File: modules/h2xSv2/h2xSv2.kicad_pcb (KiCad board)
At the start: 2 copper layers, 40.6 x 40.6 mm, 14 parts, among them J1 Conn_01x10_Male, J10 Conn_01x02_Male, J2 Conn_01x10_Male, J3 Conn_01x10_Male, J4 Conn_01x10_Male, J5 Conn_01x04_Male, J6 Conn_01x04_Male, J7 Conn_01x12_Male, J8 Conn_01x12_Male, J9 Conn_01x12_Male

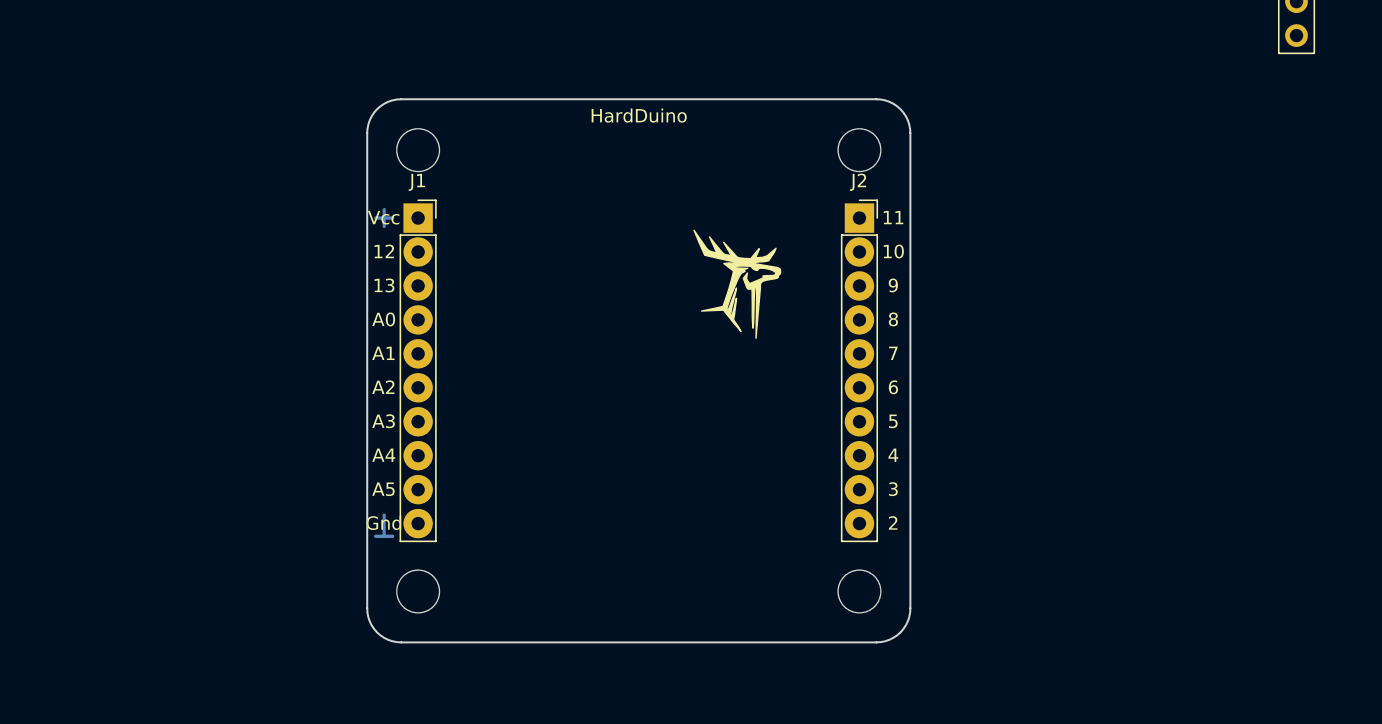
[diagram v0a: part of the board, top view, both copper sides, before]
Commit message: Fix holes and edges
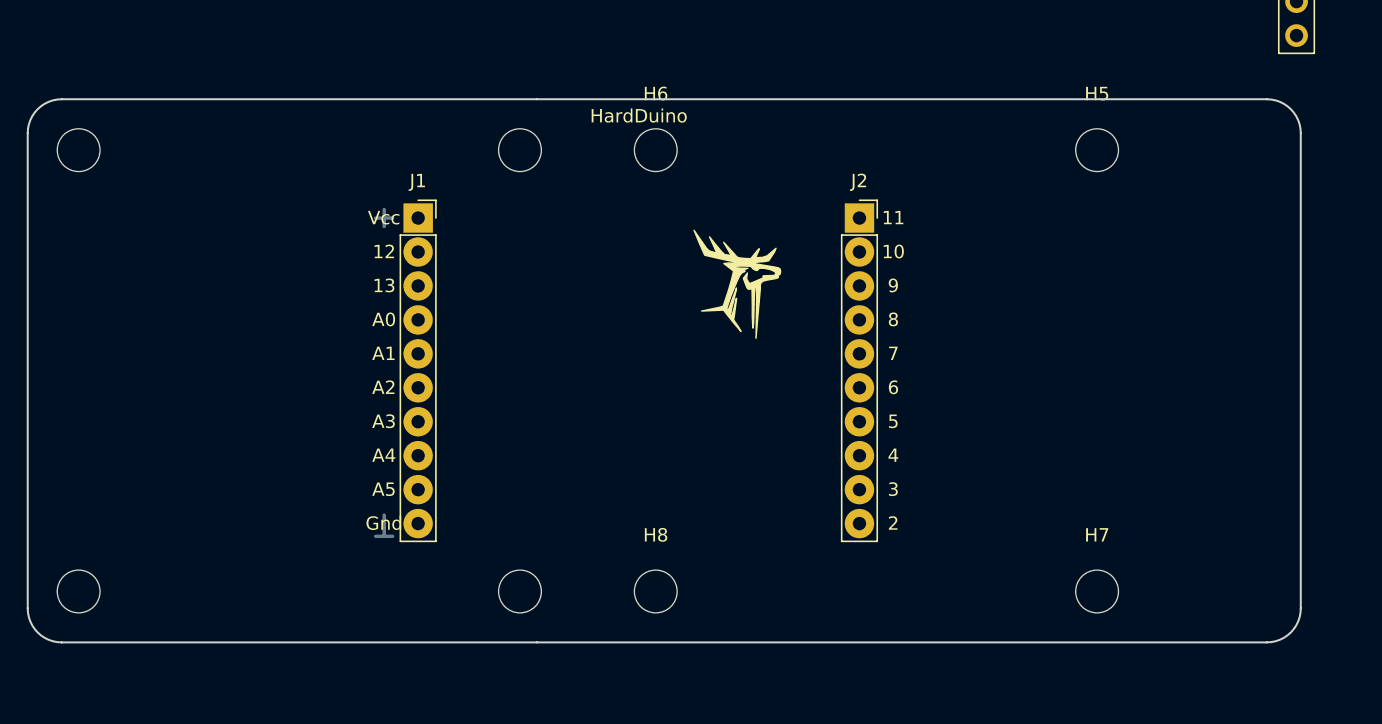
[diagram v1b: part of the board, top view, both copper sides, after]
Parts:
- added H5: MountingHole, MountingHole:MountingHole_3.2mm_M3, F.Cu at (143.5, 54.6)
- added H6: MountingHole, MountingHole:MountingHole_3.2mm_M3, F.Cu at (110.5, 54.6)
- added H7: MountingHole, MountingHole:MountingHole_3.2mm_M3, F.Cu at (143.5, 87.6)
- added H8: MountingHole, MountingHole:MountingHole_3.2mm_M3, F.Cu at (110.5, 87.6)
- moved H3 58.4 mm to (67.3, 54.6), turned to 90 degrees
- moved H4 41.7 mm to (100.3, 54.6), turned to 90 degrees
- moved H1 41.7 mm to (67.3, 87.6), turned to 90 degrees
- moved H2 7.62 mm to (100.3, 87.6), turned to 90 degrees
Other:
- board size 40.6 x 40.6 mm -> 95.2 x 40.6 mm
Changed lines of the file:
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@@
   (general
     (thickness 1.6)
-    (drawings 30)
+    (drawings 32)
     (tracks 4)
     (zones 0)
-    (modules 14)
+    (modules 18)
     (nets 21)
   )
@@
   )
   (module MountingHole:MountingHole_3.2mm_M3 (layer F.Cu)
-    (at 92.71 54.61)
+    (at 67.31 87.63 90)
     (descr "Mounting Hole 3.2mm, no annular, M3")
     (tags "mounting hole 3.2mm no annular m3")
@@
   )
   (module MountingHole:MountingHole_3.2mm_M3 (layer F.Cu)
-    (at 92.71 87.63)
+    (at 100.33 87.63 90)
     (descr "Mounting Hole 3.2mm, no annular, M3")
     (tags "mounting hole 3.2mm no annular m3")
@@
   )
   (module MountingHole:MountingHole_3.2mm_M3 (layer F.Cu)
-    (at 125.73 54.61)
+    (at 67.31 54.61 90)
     (descr "Mounting Hole 3.2mm, no annular, M3")
     (tags "mounting hole 3.2mm no annular m3")
@@
   )
   (module MountingHole:MountingHole_3.2mm_M3 (layer F.Cu)
-    (at 125.73 87.63)
+    (at 100.33 54.61 90)
     (descr "Mounting Hole 3.2mm, no annular, M3")
     (tags "mounting hole 3.2mm no annular m3")
@@
     )
   )
+  (module MountingHole:MountingHole_3.2mm_M3 (layer F.Cu)
+    (at 143.51 54.61)
+    (descr "Mounting Hole 3.2mm, no annular, M3")
+    (tags "mounting hole 3.2mm no annular m3")
+    (attr virtual)
+    (fp_text reference H5 (at 0 -4.2) (layer F.SilkS)
+      (effects (font (size 1 1) (thickness 0.15)))
+    )
+    (fp_text value MountingHole (at 0 4.2) (layer F.Fab)
+      (effects (font (size 1 1) (thickness 0.15)))
+    )
+    (fp_circle (center 0 0) (end 3.45 0) (layer F.CrtYd) (width 0.05))
+    (fp_circle (center 0 0) (end 3.2 0) (layer Cmts.User) (width 0.15))
+    (fp_text user %R (at 0.3 0) (layer F.Fab)
+      (effects (font (size 1 1) (thickness 0.15)))
+    )
+    (pad 1 np_thru_hole circle (at 0 0) (size 3.2 3.2) (drill 3.2) (layers *.Cu *.Mask))
+  )
+  (module MountingHole:MountingHole_3.2mm_M3 (layer F.Cu)
+    (at 110.49 54.61)
+    (descr "Mounting Hole 3.2mm, no annular, M3")
+    (tags "mounting hole 3.2mm no annular m3")
+    (attr virtual)
+    (fp_text reference H6 (at 0 -4.2) (layer F.SilkS)
+      (effects (font (size 1 1) (thickness 0.15)))
+    )
+    (fp_text value MountingHole (at 0 4.2) (layer F.Fab)
+      (effects (font (size 1 1) (thickness 0.15)))
+    )
+    (fp_text user %R (at 0.3 0) (layer F.Fab)
+      (effects (font (size 1 1) (thickness 0.15)))
+    )
+    (fp_circle (center 0 0) (end 3.2 0) (layer Cmts.User) (width 0.15))
+    (fp_circle (center 0 0) (end 3.45 0) (layer F.CrtYd) (width 0.05))
+    (pad 1 np_thru_hole circle (at 0 0) (size 3.2 3.2) (drill 3.2) (layers *.Cu *.Mask))
+  )
+  (module MountingHole:MountingHole_3.2mm_M3 (layer F.Cu)
+    (at 143.51 87.63)
+    (descr "Mounting Hole 3.2mm, no annular, M3")
+    (tags "mounting hole 3.2mm no annular m3")
+    (attr virtual)
+    (fp_text reference H7 (at 0 -4.2) (layer F.SilkS)
+      (effects (font (size 1 1) (thickness 0.15)))
+    )
+    (fp_text value MountingHole (at 0 4.2) (layer F.Fab)
+      (effects (font (size 1 1) (thickness 0.15)))
+    )
+    (fp_circle (center 0 0) (end 3.45 0) (layer F.CrtYd) (width 0.05))
+    (fp_circle (center 0 0) (end 3.2 0) (layer Cmts.User) (width 0.15))
+    (fp_text user %R (at 0.3 0) (layer F.Fab)
+      (effects (font (size 1 1) (thickness 0.15)))
+    )
+    (pad 1 np_thru_hole circle (at 0 0) (size 3.2 3.2) (drill 3.2) (layers *.Cu *.Mask))
+  )
+  (module MountingHole:MountingHole_3.2mm_M3 (layer F.Cu)
+    (at 110.49 87.63)
+    (descr "Mounting Hole 3.2mm, no annular, M3")
+    (tags "mounting hole 3.2mm no annular m3")
+    (attr virtual)
+    (fp_text reference H8 (at 0 -4.2) (layer F.SilkS)
+      (effects (font (size 1 1) (thickness 0.15)))
+    )
+    (fp_text value MountingHole (at 0 4.2) (layer F.Fab)
+      (effects (font (size 1 1) (thickness 0.15)))
+    )
+    (fp_text user %R (at 0.3 0) (layer F.Fab)
+      (effects (font (size 1 1) (thickness 0.15)))
+    )
+    (fp_circle (center 0 0) (end 3.2 0) (layer Cmts.User) (width 0.15))
+    (fp_circle (center 0 0) (end 3.45 0) (layer F.CrtYd) (width 0.05))
+    (pad 1 np_thru_hole circle (at 0 0) (size 3.2 3.2) (drill 3.2) (layers *.Cu *.Mask))
+  )
   (gr_poly (pts (xy 113.35 60.6) (xy 114.06 61.62) (xy 114.28 61.94) (xy 114.47 62.12) (xy 114.53 62.16) (xy 114.96 62.29) (xy 115 62.27) (xy 115 62.18) (xy 114.81 61.75) (xy 114.51 61.1) (xy 115.32 62.09) (xy 115.52 62.31) (xy 115.64 62.41) (xy 115.72 62.44) (xy 115.9 62.45) (xy 116.12 62.51) (xy 116.08 62.39) (xy 115.57 61.5) (xy 116.34 62.34) (xy 116.5 62.53) (xy 116.59 62.61) (xy 116.7 62.66) (xy 117.14 62.71) (xy 117.6 62.73) (xy 118.08 62.13) (xy 118.23 61.98) (xy 118.22 62.06) (xy 118.08 62.39) (xy 118 62.56) (xy 117.99 62.64) (xy 118.07 62.65) (xy 118.47 62.63) (xy 118.82 62.52) (xy 119.49 61.95) (xy 119.37 62.24) (xy 118.94 62.89) (xy 118.61 62.95) (xy 118 63) (xy 117.81 63.07) (xy 118.03 63.13) (xy 119.36 63.35) (xy 119.68 63.42) (xy 119.81 63.52) (xy 119.83 63.69) (xy 119.81 63.85) (xy 119.75 63.93) (xy 119.7 63.95) (xy 119.66 64.03) (xy 119.66 64.13) (xy 119.6 64.18) (xy 119.41 64.23) (xy 118.79 64.34) (xy 118.5 64.42) (xy 118.37 64.54) (xy 118.34 64.6) (xy 118.31 64.75) (xy 118.32 64.92) (xy 117.99 68.69) (xy 118.04 65.3) (xy 118.03 65.02) (xy 118.02 64.83) (xy 118.01 64.79) (xy 117.97 64.75) (xy 117.92 64.87) (xy 117.89 65.2) (xy 117.86 65.69) (xy 117.83 67.07) (xy 117.81 67.6) (xy 117.77 67.93) (xy 117.74 67.75) (xy 117.71 67.07) (xy 117.71 66.19) (xy 117.69 64.97) (xy 117.53 65.01) (xy 117.42 65.01) (xy 117.35 64.96) (xy 117.28 64.83) (xy 117.04 64.2) (xy 117.35 63.8) (xy 117.31 64.03) (xy 117.3 64.19) (xy 117.3 64.26) (xy 117.37 64.39) (xy 117.52 64.6) (xy 118.43 64.21) (xy 118.56 64.14) (xy 118.61 64.08) (xy 118.5 64.04) (xy 118.71 64) (xy 119.23 63.99) (xy 119.35 63.97) (xy 119.44 63.92) (xy 119.47 63.86) (xy 119.44 63.74) (xy 119.28 63.64) (xy 119.01 63.53) (xy 118.61 63.45) (xy 118.37 63.44) (xy 118.23 63.46) (xy 118.18 63.5) (xy 118.11 63.6) (xy 118.06 63.61) (xy 118 63.61) (xy 117.88 63.56) (xy 117.73 63.46) (xy 117.69 63.4) (xy 117.68 63.36) (xy 117.62 63.33) (xy 117.54 63.3) (xy 117.05 63.28) (xy 116.6 63.29) (xy 116.46 63.31) (xy 116.34 63.34) (xy 116.36 63.38) (xy 116.57 63.42) (xy 116.87 63.44) (xy 117.38 63.45) (xy 116.96 63.6) (xy 116.96 63.63) (xy 117.16 63.65) (xy 117.17 63.68) (xy 116.93 63.8) (xy 116.87 63.87) (xy 116.74 64.06) (xy 116.54 64.49) (xy 116.11 65.54) (xy 115.89 66.19) (xy 115.84 66.36) (xy 115.81 66.5) (xy 115.86 66.58) (xy 115.91 66.55) (xy 115.95 66.48) (xy 116.04 66.26) (xy 116.22 65.75) (xy 116.53 64.92) (xy 116.49 65.18) (xy 116.24 66.18) (xy 116.18 66.39) (xy 116.12 66.73) (xy 116.1 66.85) (xy 116.1 66.96) (xy 116.15 67.02) (xy 116.21 66.94) (xy 116.25 66.79) (xy 116.35 66.42) (xy 116.51 65.7) (xy 116.54 65.7) (xy 116.39 66.86) (xy 116.32 67.31) (xy 116.71 67.88) (xy 116.87 68.18) (xy 116.26 67.47) (xy 115.56 66.58) (xy 113.92 66.65) (xy 115.32 66.35) (xy 115.53 66.28) (xy 115.61 66.06) (xy 115.9 65.18) (xy 116.15 64.33) (xy 116.31 63.66) (xy 115.58 63.09) (xy 115.94 63.05) (xy 116.39 63.07) (xy 116.87 63.08) (xy 114.95 62.66) (xy 114.15 62.47) (xy 113.72 61.5)) (layer F.SilkS) (width 0.1))
   (gr_text HardDuino (at 109.22 52.07) (layer F.SilkS)
@@
     (effects (font (size 1 1) (thickness 0.15)))
   )
-  (gr_arc (start 127 53.34) (end 129.54 53.34) (angle -90) (layer Edge.Cuts) (width 0.15))
-  (gr_arc (start 127 88.9) (end 127 91.44) (angle -90) (layer Edge.Cuts) (width 0.15))
-  (gr_arc (start 91.44 88.9) (end 88.9 88.9) (angle -90) (layer Edge.Cuts) (width 0.15))
-  (gr_arc (start 91.44 53.34) (end 91.44 50.8) (angle -90) (layer Edge.Cuts) (width 0.15))
-  (gr_line (start 88.9 88.9) (end 88.9 53.34) (layer Edge.Cuts) (width 0.15))
-  (gr_line (start 127 91.44) (end 91.44 91.44) (layer Edge.Cuts) (width 0.15))
-  (gr_line (start 129.54 53.34) (end 129.54 88.9) (layer Edge.Cuts) (width 0.15))
-  (gr_line (start 91.44 50.8) (end 127 50.8) (layer Edge.Cuts) (width 0.15))
+  (gr_line (start 101.6 91.44) (end 156.21 91.44) (layer Edge.Cuts) (width 0.15))
+  (gr_line (start 101.6 50.8) (end 156.21 50.8) (layer Edge.Cuts) (width 0.15))
+  (gr_arc (start 66.04 53.34) (end 66.04 50.8) (angle -90) (layer Edge.Cuts) (width 0.15))
+  (gr_arc (start 156.21 53.34) (end 158.75 53.34) (angle -90) (layer Edge.Cuts) (width 0.15))
+  (gr_arc (start 156.21 88.9) (end 156.21 91.44) (angle -90) (layer Edge.Cuts) (width 0.15))
+  (gr_arc (start 66.04 88.9) (end 63.5 88.9) (angle -90) (layer Edge.Cuts) (width 0.15))
+  (gr_line (start 101.6 91.44) (end 66.04 91.44) (layer Edge.Cuts) (width 0.15))
+  (gr_line (start 158.75 53.34) (end 158.75 88.9) (layer Edge.Cuts) (width 0.15))
+  (gr_line (start 66.04 50.8) (end 101.6 50.8) (layer Edge.Cuts) (width 0.15))
+  (gr_line (start 63.5 88.9) (end 63.5 53.34) (layer Edge.Cuts) (width 0.15))
   (segment (start 90.17 81.915) (end 90.17 83.5025) (width 0.25) (layer B.Cu) (net 0))
   (segment (start 89.535 83.5025) (end 90.805 83.5025) (width 0.25) (layer B.Cu) (net 0))

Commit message: Place pinheaders
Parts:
- moved J5 109.9 mm to (148.6, 55.9)
- moved J6 103.5 mm to (148.6, 52.7)
- moved J10 80.7 mm to (67.3, 64.1), turned to 180 degrees
- moved J9 72.7 mm to (156.2, 88.9), turned to 180 degrees
- moved J8 71.7 mm to (153.7, 88.9), turned to 180 degrees
- moved J7 71.2 mm to (151.1, 88.9), turned to 180 degrees
- moved J4 68.3 mm to (138.4, 87.6), turned to 270 degrees
- moved J3 64.2 mm to (138.4, 54.6), turned to 270 degrees
- moved J2 41.3 mm to (95.2, 87.6), turned to 270 degrees
- moved J1 5.68 mm to (95.2, 54.6), turned to 270 degrees
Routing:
- net (no net): track 5.40 -> 2.86 mm
- net /A2: track 0.00 -> 2.54 mm
